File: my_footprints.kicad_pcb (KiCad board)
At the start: 2 copper layers, 3 parts

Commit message: nuevas huellas
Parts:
- added REF**: JST_SH_BM06B-SRSS-TB_06x1.00mm_Straight, Connectors_JST:JST_SH_BM06B-SRSS-TB_06x1.00mm_Straight, F.Cu at (130.6, 70.4)
- added REF**: JST_SH_SM06B-SRSS-TB_06x1.00mm_Angled, Connectors_JST:JST_SH_SM06B-SRSS-TB_06x1.00mm_Angled, F.Cu at (171.8, 67.6)
- added REF**: GPS_em506, footprints:GPS_em506_size, F.Cu at (158.0, 103.7)
- moved REF** 24.7 mm to (29.9, 61.8), turned to 0 degrees

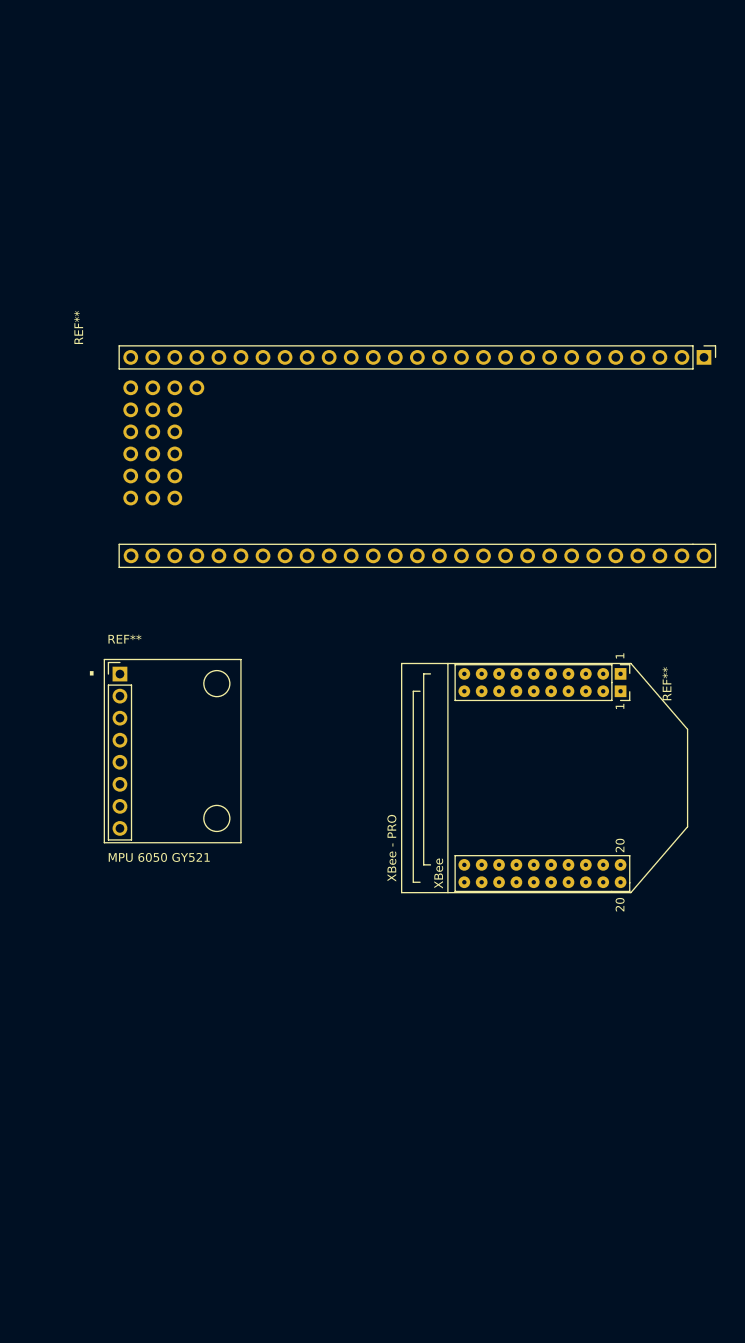
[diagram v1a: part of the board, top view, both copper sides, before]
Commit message: testpoints footprints
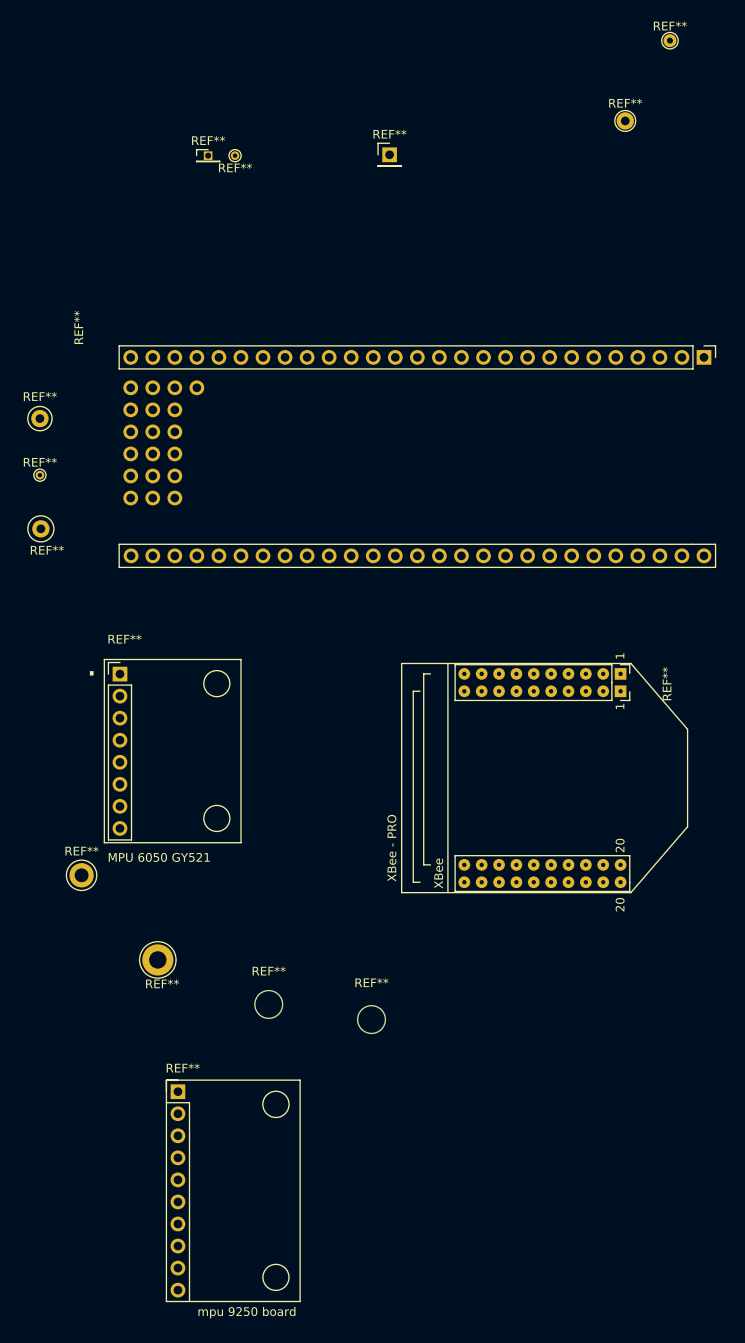
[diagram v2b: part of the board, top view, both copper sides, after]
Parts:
- added REF**: TestPoint_THTPad_D1.0mm_Drill0.5mm, TestPoint:TestPoint_THTPad_D1.0mm_Drill0.5mm, F.Cu at (43.2, 2.10)
- added REF**: MountingHole_3.2mm_M3_DIN965, Mounting_Holes:MountingHole_3.2mm_M3_DIN965, F.Cu at (47.1, 99.9)
- added REF**: TestPoint_Keystone_5000-5004_Miniature, TestPoint:TestPoint_Keystone_5000-5004_Miniature, F.Cu at (20.7, 32.4)
- added REF**: TestPoint_Keystone_5005-5009_Compact, TestPoint:TestPoint_Keystone_5005-5009_Compact, F.Cu at (25.5, 85.0)
- added REF**: TestPoint_THTPad_D1.0mm_Drill0.5mm, TestPoint:TestPoint_THTPad_D1.0mm_Drill0.5mm, F.Cu at (20.7, 38.9)
- added REF**: TestPoint_Loop_D2.50mm_Drill1.0mm, TestPoint:TestPoint_Loop_D2.50mm_Drill1.0mm, F.Cu at (20.8, 45.1)
- added REF**: Socket_Strip_Straight_1x01_Pitch1.27mm, Socket_Strips:Socket_Strip_Straight_1x01_Pitch1.27mm, F.Cu at (40.1, 2.10)
- added REF**: TestPoint_Loop_D3.80mm_Drill2.0mm, TestPoint:TestPoint_Loop_D3.80mm_Drill2.0mm, F.Cu at (34.3, 94.8)
- added REF**: TestPoint_THTPad_D1.5mm_Drill0.7mm, TestPoint:TestPoint_THTPad_D1.5mm_Drill0.7mm, F.Cu at (93.3, -11.2)
- added REF**: Socket_Strip_Straight_1x01_Pitch2.54mm, Socket_Strips:Socket_Strip_Straight_1x01_Pitch2.54mm, F.Cu at (61.0, 2.00)
- added REF**: TestPoint_THTPad_D2.0mm_Drill1.0mm, TestPoint:TestPoint_THTPad_D2.0mm_Drill1.0mm, F.Cu at (88.2, -1.90)
- added REF**: acc_mpu9250, footprints:mpu9250_board, F.Cu at (36.6, 109.9)
- added REF**: MountingHole_3.2mm_M3, Mounting_Holes:MountingHole_3.2mm_M3, F.Cu at (58.9, 101.6)

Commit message: modificacion footprint mpu9250, agregados agujeros
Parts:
- removed the REF** at (43.2, 2.10)
- removed the REF** at (47.1, 99.9)
- removed the REF** at (20.7, 32.4)
- removed the REF** at (25.5, 85.0)
- removed the REF** at (20.7, 38.9)
- removed the REF** at (20.8, 45.1)
- removed the REF** at (40.1, 2.10)
- removed the REF** at (34.3, 94.8)
- removed the REF** at (93.3, -11.2)
- removed the REF** at (61.0, 2.00)
- removed the REF** at (88.2, -1.90)
- removed the REF** at (97.2, 25.3)
- removed the REF** at (87.6, 63.8)
- removed the REF** at (29.9, 61.8)
- removed the REF** at (130.6, 70.4)
- removed the REF** at (171.8, 67.6)
- removed the REF** at (158.0, 103.7)
- removed the REF** at (36.6, 109.9)
- removed the REF** at (58.9, 101.6)
- added REF**: XBEE-20_THT, footprints:XBEE-20_THT, F.Cu at (172.7, 77.2)
- added REF**: XBee_xb24cz7pit-004, footprints:xbee_xb24cz7pit_004, F.Cu at (211.3, 64.8)
- added REF**: XBEE-20_THT, footprints:XBEE-20_THT, F.Cu at (141.8, 42.9)
- added REF**: lpc1769_stick_revC, footprints:lpc1769_board_revC, F.Cu at (45.0, 97.1)
- added REF**: XBee_xb24cz7pit-004, footprints:xbee_xb24cz7pit_004, F.Cu at (197.8, 85.8)
- added REF**: lpc1769_stick_revC, footprints:lpc1769_board_revC, F.Cu at (85.3, 97.2)
- added REF**: XBEE-20_THT, footprints:XBEE-20_THT, F.Cu at (142.4, 77.0)
- added REF**: XBee_xb24cz7pit-004, footprints:xbee_xb24cz7pit_004, F.Cu at (229.2, 85.8)
- added U1: acc_mpu9250_board, footprints:mpu9250_board, F.Cu at (185.9, 121.0)
- added U1: acc_mpu9250_board, footprints:mpu9250_board, F.Cu at (160.3, 121.1)
- added U1: acc_mpu9250_board, footprints:mpu9250_board, F.Cu at (132.2, 121.1)

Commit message: corrección M3 del mpu9250
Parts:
- removed the U1 at (185.9, 121.0)
- removed the U1 at (160.3, 121.1)
- removed the U1 at (132.2, 121.1)
- added U1: acc_mpu9250_board, footprints:mpu9250_board, F.Cu at (181.5, 126.5)
- added U1: acc_mpu9250_board, footprints:mpu9250_board, F.Cu at (160.3, 125.9)
- added U1: acc_mpu9250_board, footprints:mpu9250_board, F.Cu at (142.2, 125.8)

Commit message: lpc update
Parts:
- removed the REF** at (45.0, 97.1)
- removed the REF** at (85.3, 97.2)
- added REF**: lpc1769_stick_revC, footprints:lpc1769_board_revC, F.Cu at (26.7, 102.9)
- added REF**: lpc1769_stick_revD, footprints:lpc1769_board_revD, F.Cu at (69.8, 104.1)

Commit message: testing
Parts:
- removed the REF** at (172.7, 77.2)
- removed the REF** at (211.3, 64.8)
- removed the REF** at (141.8, 42.9)
- removed the REF** at (197.8, 85.8)
- removed the REF** at (142.4, 77.0)
- removed the REF** at (229.2, 85.8)
- removed the REF** at (69.8, 104.1)
- removed U1 (x3): acc_mpu9250_board, footprints:mpu9250_board
- added XA**: Arduino_Mega2560_Shield, Arduino:Arduino_Mega2560_Shield, F.Cu at (61.0, 83.8)
- moved REF** 49.5 mm to (76.2, 104.1)

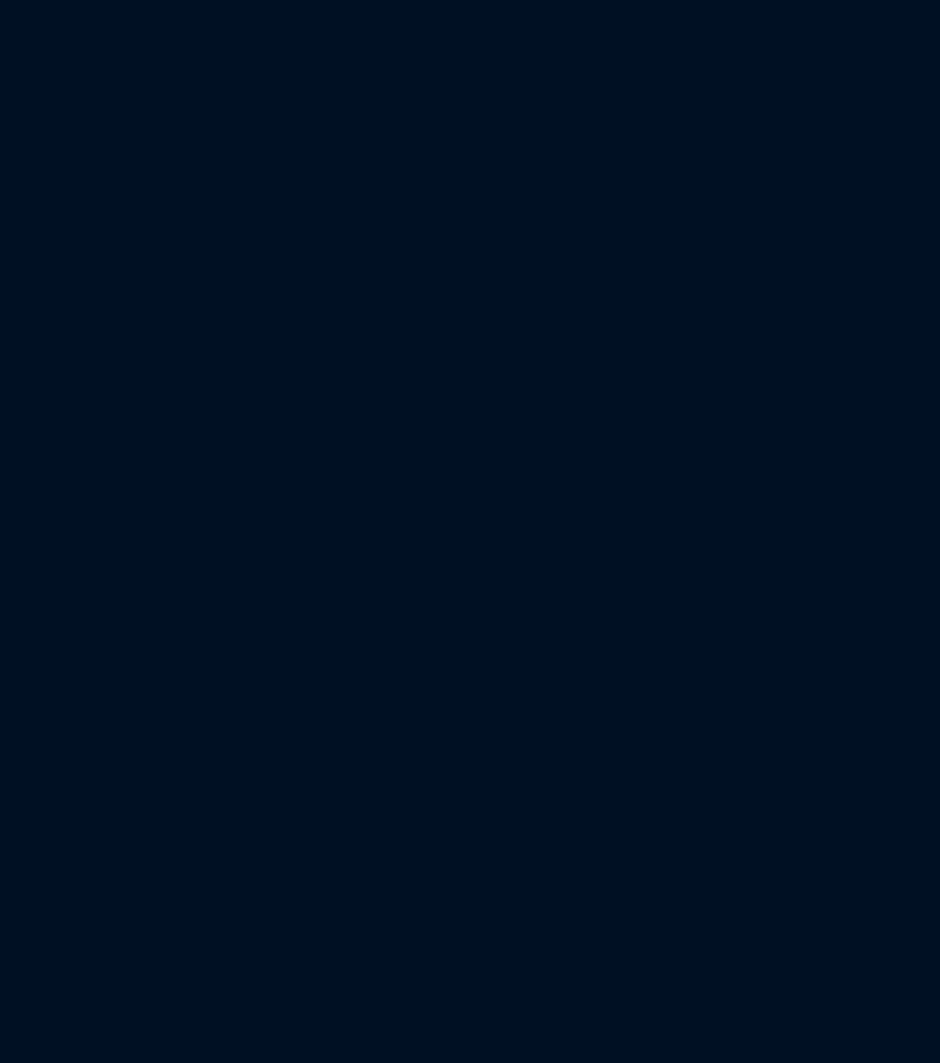
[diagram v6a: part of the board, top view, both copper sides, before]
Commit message: sd card added
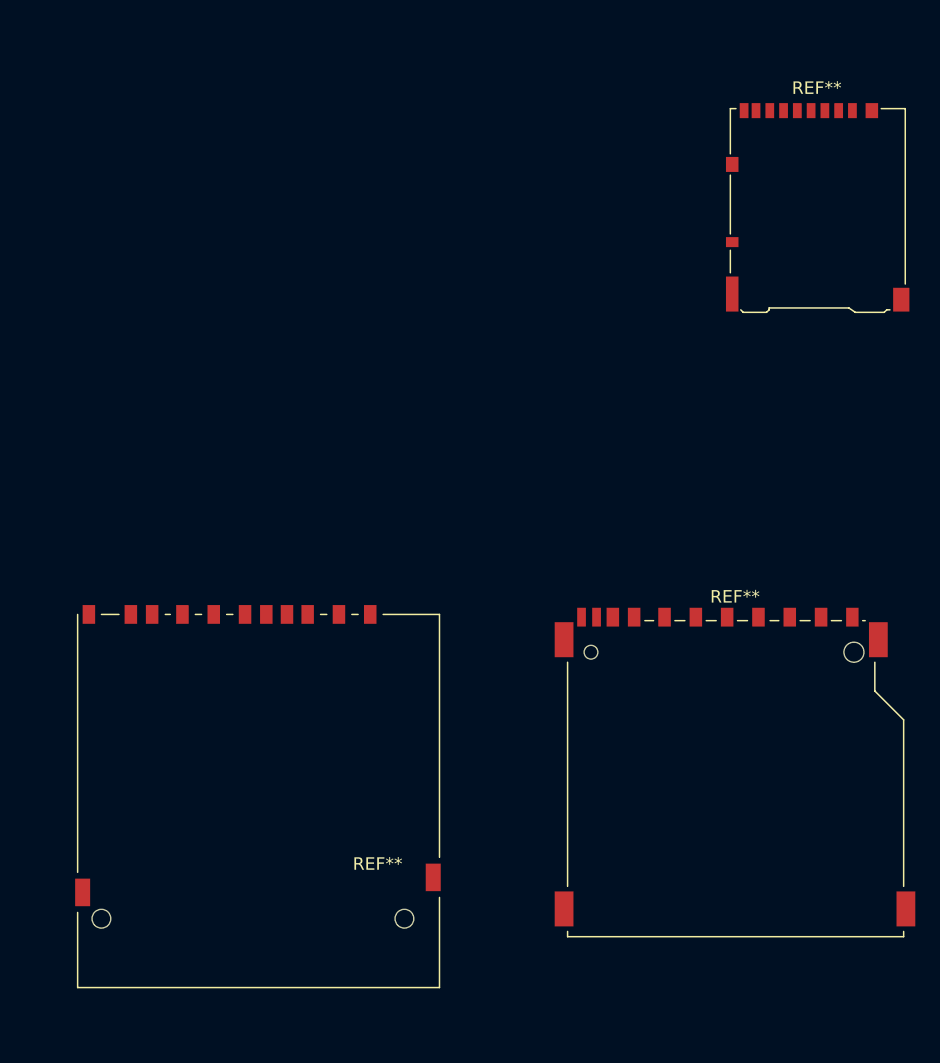
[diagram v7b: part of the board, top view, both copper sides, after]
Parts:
- added REF**: SD_TE_2041021, Connector_Card:SD_TE_2041021, F.Cu at (223.5, 117.9)
- added REF**: SD_Card_Receptacle, Connectors:SD_Card_Receptacle, F.Cu at (185.4, 117.8)
- added REF**: microSD_HC_Hirose_DM3AT-SF-PEJM5, Connector_Card:microSD_HC_Hirose_DM3AT-SF-PEJM5, F.Cu at (230.1, 73.2)

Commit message: cambios
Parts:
- added XA**: Arduino_Mega2560_Shield, Arduino:Arduino_Mega2560_Shield_flippedONtop, F.Cu at (332.0, 59.4)
